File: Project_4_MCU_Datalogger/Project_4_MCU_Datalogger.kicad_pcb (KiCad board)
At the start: 2 copper layers, 29 parts, among them J1 Conn_01x04_Pin, J2 Conn_01x09_Pin, J3 Conn_01x04_Pin, J4 Conn_02x03_Odd_Even, U1 24LC1025, U2 DS1337S_, U3 24LC1025, U4 ATMEGA328P-AU, Y1 32.768 KHz, Y2 16 MHz

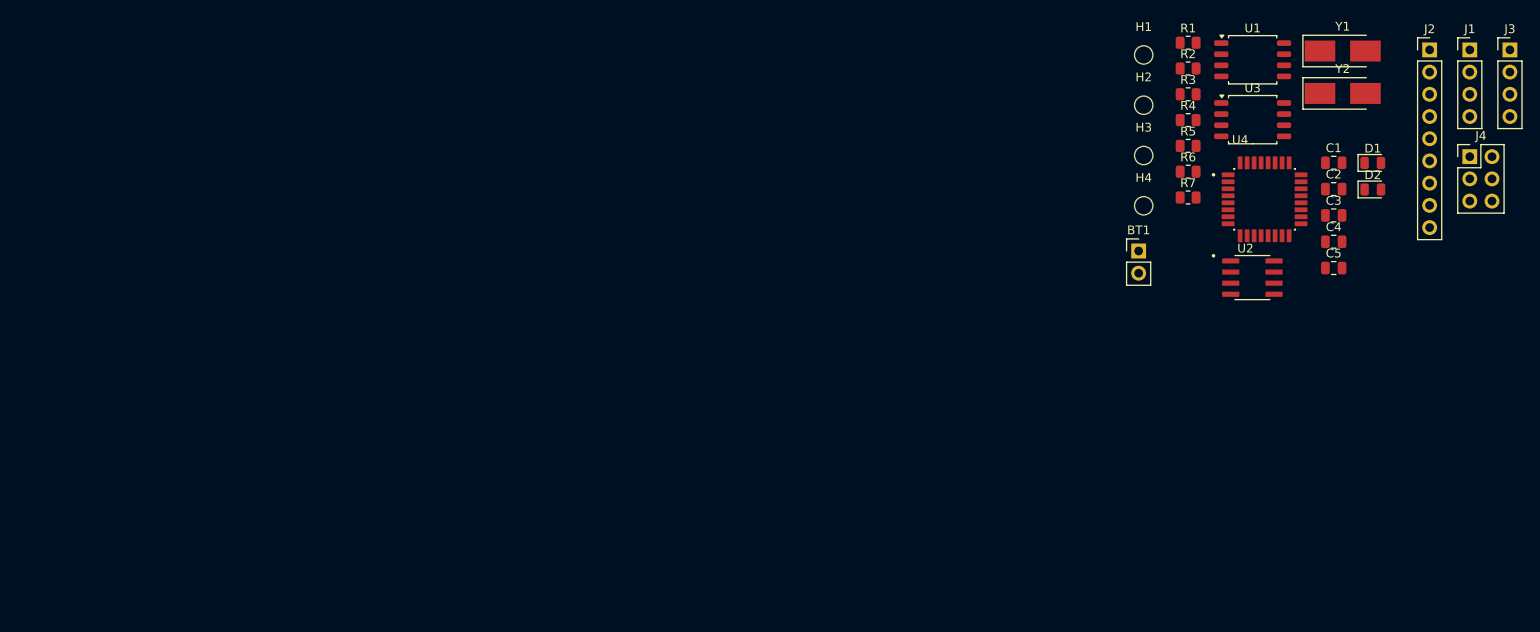
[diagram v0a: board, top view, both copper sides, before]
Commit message: completed placement of footprints
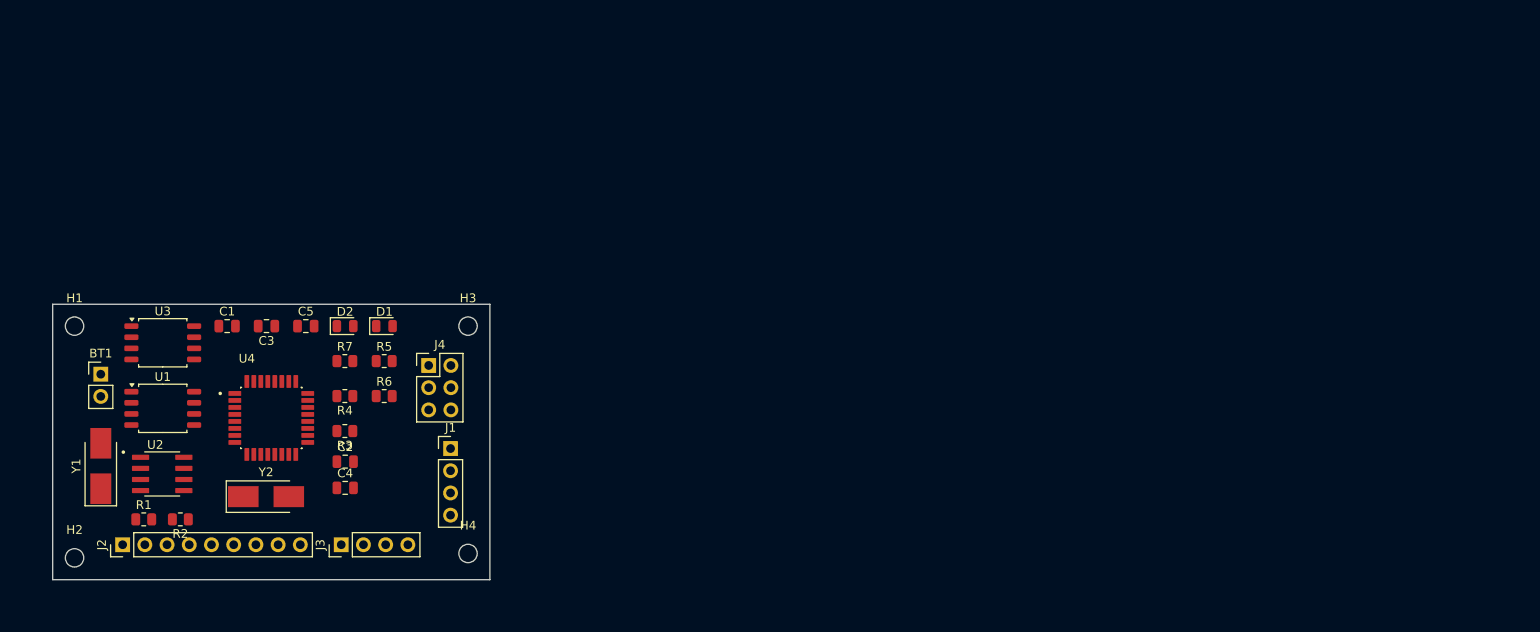
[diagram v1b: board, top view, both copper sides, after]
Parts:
- moved J2 159.8 mm to (108.0, 97.5), turned to 90 degrees
- moved Y1 149.7 mm to (105.5, 88.5), turned to 90 degrees
- moved J3 145.1 mm to (133.0, 97.5), turned to 90 degrees
- moved H2 132.8 mm to (102.5, 99.0)
- moved Y2 131.5 mm to (124.4, 92.0)
- moved R1 131.3 mm to (110.4, 94.6)
- moved U1 130.9 mm to (112.6, 81.9)
- moved C1 127.9 mm to (120.0, 72.5)
- moved U3 127.2 mm to (112.6, 74.4)
- moved U2 126.7 mm to (112.5, 89.4)
- moved R2 126.3 mm to (114.6, 94.6), turned to 180 degrees
- moved H1 126.1 mm to (102.5, 72.5)
- moved J1 125.2 mm to (145.5, 86.5)
- moved C3 122.7 mm to (124.5, 72.5), turned to 180 degrees
- moved J4 121.4 mm to (143.0, 77.0)
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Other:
- board outline added: 50 x 31.5 mm

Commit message: pcb completed
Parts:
- added REF**: KiCad-Logo2_5mm_SilkScreen, Symbol:KiCad-Logo2_5mm_SilkScreen, B.Cu at (103.8, 91.2)
- moved C3 22.2 mm to (127.0, 94.5)
- moved C1 15.7 mm to (114.0, 87.0), turned to 180 degrees
- moved C2 14.1 mm to (121.0, 94.5)
- moved R3 14.0 mm to (123.3, 74.8), turned to 0 degrees
- moved C5 12.7 mm to (132.7, 84.6)
- moved R4 8.49 mm to (127.2, 74.8)
- moved C4 8.43 mm to (132.7, 82.6)
- moved H4 3.91 mm to (150.0, 101.5)
- moved H1 3.54 mm to (100.0, 70.0)
- moved H2 3.54 mm to (100.0, 101.5)
- moved H3 3.54 mm to (150.0, 70.0)
- moved D2 2.37 mm to (132.7, 74.8)
- moved R7 2.37 mm to (132.7, 78.8)
- moved D1 2.25 mm to (137.9, 74.8)
- moved R5 2.25 mm to (137.9, 78.8)
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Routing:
- net /SCL: track 0.00 -> 90.7 mm
- net /SDA: track 0.00 -> 80.4 mm, vias 0 -> 2
- net /TX: track 0.00 -> 35.3 mm, vias 0 -> 2
- net /RX: track 0.00 -> 32.9 mm, vias 0 -> 2
- net /D2: track 0.00 -> 31.9 mm, vias 0 -> 1
- net /SCK: track 0.00 -> 27.5 mm, vias 0 -> 1
- net /D3: track 0.00 -> 27.5 mm, vias 0 -> 1
- net /MISO: track 0.00 -> 26.6 mm, vias 0 -> 1
- net /MOSI: track 0.00 -> 26.5 mm
- net /D7: track 0.00 -> 26.5 mm, vias 0 -> 2
- net GND: track 0.00 -> 25.4 mm, vias 0 -> 17
- net /D8: track 0.00 -> 24.4 mm
- net /D4: track 0.00 -> 23.5 mm, vias 0 -> 1
- net /RESET: track 0.00 -> 21.9 mm, vias 0 -> 2
- net /D5: track 0.00 -> 17.4 mm, vias 0 -> 1
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- added copper zone on B.Cu, net GND
- added copper zone on F.Cu, net VCC
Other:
- board size 50 x 31.5 mm -> 58 x 39.5 mm
- board text added: "2"
- board text added: "3"
- board text added: "4"
- board text added: "5"
- board text added: "6"
- board text added: "7"
- board text added: "8"
- board text added: "GND"
- board text added: "ICSP"
- board text added: "ISCP"
- board text added: "MISO"
- board text added: "MOSI"
- board text added: "RESET"
- board text added: "RX"
- board text added: "SCK"
- board text added: "SCL"
- board text added: "SDA"
- board text added: "TX"
- board text added: "VCC"
- board text added: "v1 Datalogger with ATMega328P - 2MBit EEPROM - RTC - I2C, SPI, GPIOs"

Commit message: pcb 4layer completed
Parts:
- moved C1 0.50 mm to (114.0, 86.5)
- moved R3 0.50 mm to (123.8, 74.8)
- moved R4 0.50 mm to (127.7, 74.8)
- moved C5 0.40 mm to (132.7, 85.0)
- moved R6 0.18 mm to (138.1, 82.8)
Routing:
- net VCC: track 15.5 -> 39.9 mm, vias 0 -> 18
- net /SCL: track 90.7 -> 73.3 mm
- net /SDA: track 80.4 -> 97.7 mm, vias 2 -> 0
- net /D7: track 26.5 -> 13.1 mm, vias 2 -> 1
- net /SCK: track 27.5 -> 38.4 mm
- net /D8: track 24.4 -> 14.2 mm, vias 0 -> 1
- net /RX: track 32.9 -> 29.0 mm, vias 2 -> 1
- net GND: track 25.4 -> 29.1 mm
- net /MISO: track 26.6 -> 23.6 mm
- net /D2: track 31.9 -> 29.1 mm
- net /D5: track 17.4 -> 14.6 mm
- net /SQW: track 5.68 -> 8.48 mm, vias 0 -> 2
- net /RESET: track 21.9 -> 24.3 mm
- net /D6: track 16.2 -> 13.8 mm
- net /D4: track 23.5 -> 22.0 mm
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- added copper zone on In1.Cu, net GND
- added copper zone on In2.Cu, net VCC
- removed copper zone on B.Cu, net GND
- removed copper zone on F.Cu, net VCC
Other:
- copper layers 2 -> 4
